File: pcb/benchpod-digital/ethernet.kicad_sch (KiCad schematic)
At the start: 41 parts, among them J7 HR911105A_C12074, U6 LAN8742AI-CZ-TR, Y1 6pF ±10ppm SMD2016-4P Crystal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

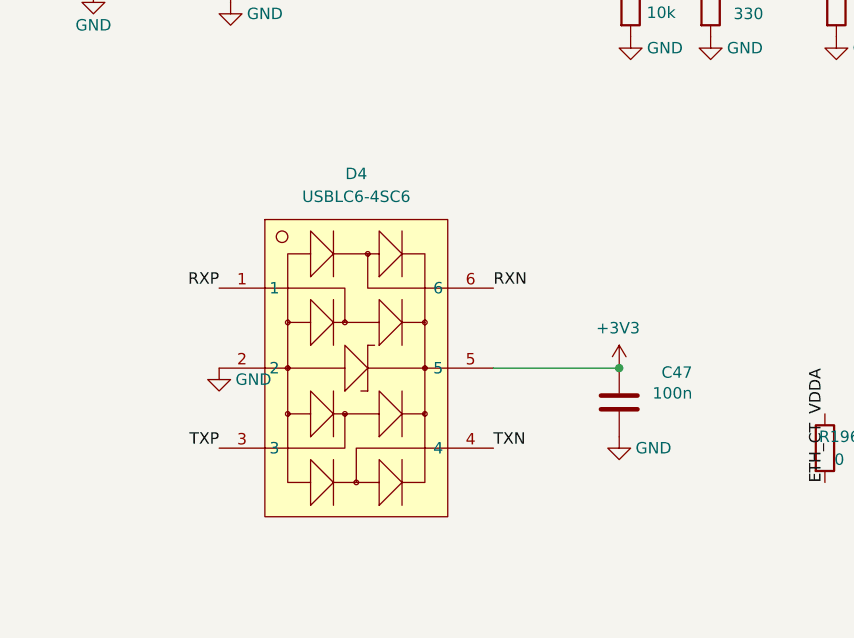
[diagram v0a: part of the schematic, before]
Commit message: digital v3r3: D4 Ethernet ESD -> TPD4E05U06DQAR (flow-through, no 3.3 V rail)
As on TI's DP83825 EVM (U3): D1 = TX pair, D2 = RX pair, each line on
both opposite pads (1/10, 2/9, 4/7, 5/6) so the pairs run straight
through the part; GND on 3 and 8. USBLC6-4SC6 clamped to +3V3 and its
SOT-23-6 pinout forced the pairs to cross; C47 (its +3V3 pin cap) removed.
Part imported with easyeda2kicad (C138714), pins set to passive.
ERC unchanged (467).

Co-Authored-By: Claude Opus 5.5 <noreply@anthropic.com>
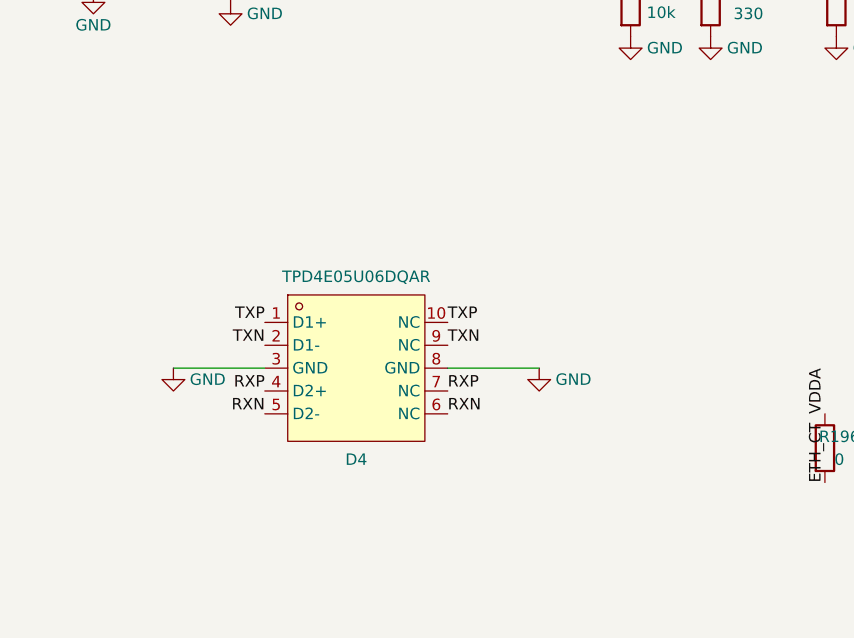
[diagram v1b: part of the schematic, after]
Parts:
- removed C47: 100n, Capacitor_SMD:C_0402_1005Metric, symbol Device:C
- removed D4: USBLC6-4SC6, lcsc:SOT-23-6_L2.9-W1.6-P0.95-LS2.8-BL, symbol lcsc_lib:USBLC6-4SC6
- added D4: TPD4E05U06DQAR, lcsc_footprints:C138714_USON-10_L2.5-W1.0-P0.50-BL, symbol lcsc_imported:TPD4E05U06DQAR
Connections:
- net GND: now also D4.3 (GND), D4.8 (GND)
- net RXN: now also D4.5 (D2-), D4.6 (NC)
- net RXP: now also D4.4 (D2+), D4.7 (NC)
- net TXN: now also D4.2 (D1-), D4.9 (NC)
- net TXP: now also D4.1 (D1+), D4.10 (NC)
